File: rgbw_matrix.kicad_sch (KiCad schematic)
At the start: 34 parts, among them IC1 TLC59283DBQR, IC2 TLC59283DBQR, IC3 TLC59283DBQR, IC4 TLC59283DBQR, IC5 TLC59283DBQR, IC6 TLC59283DBQR

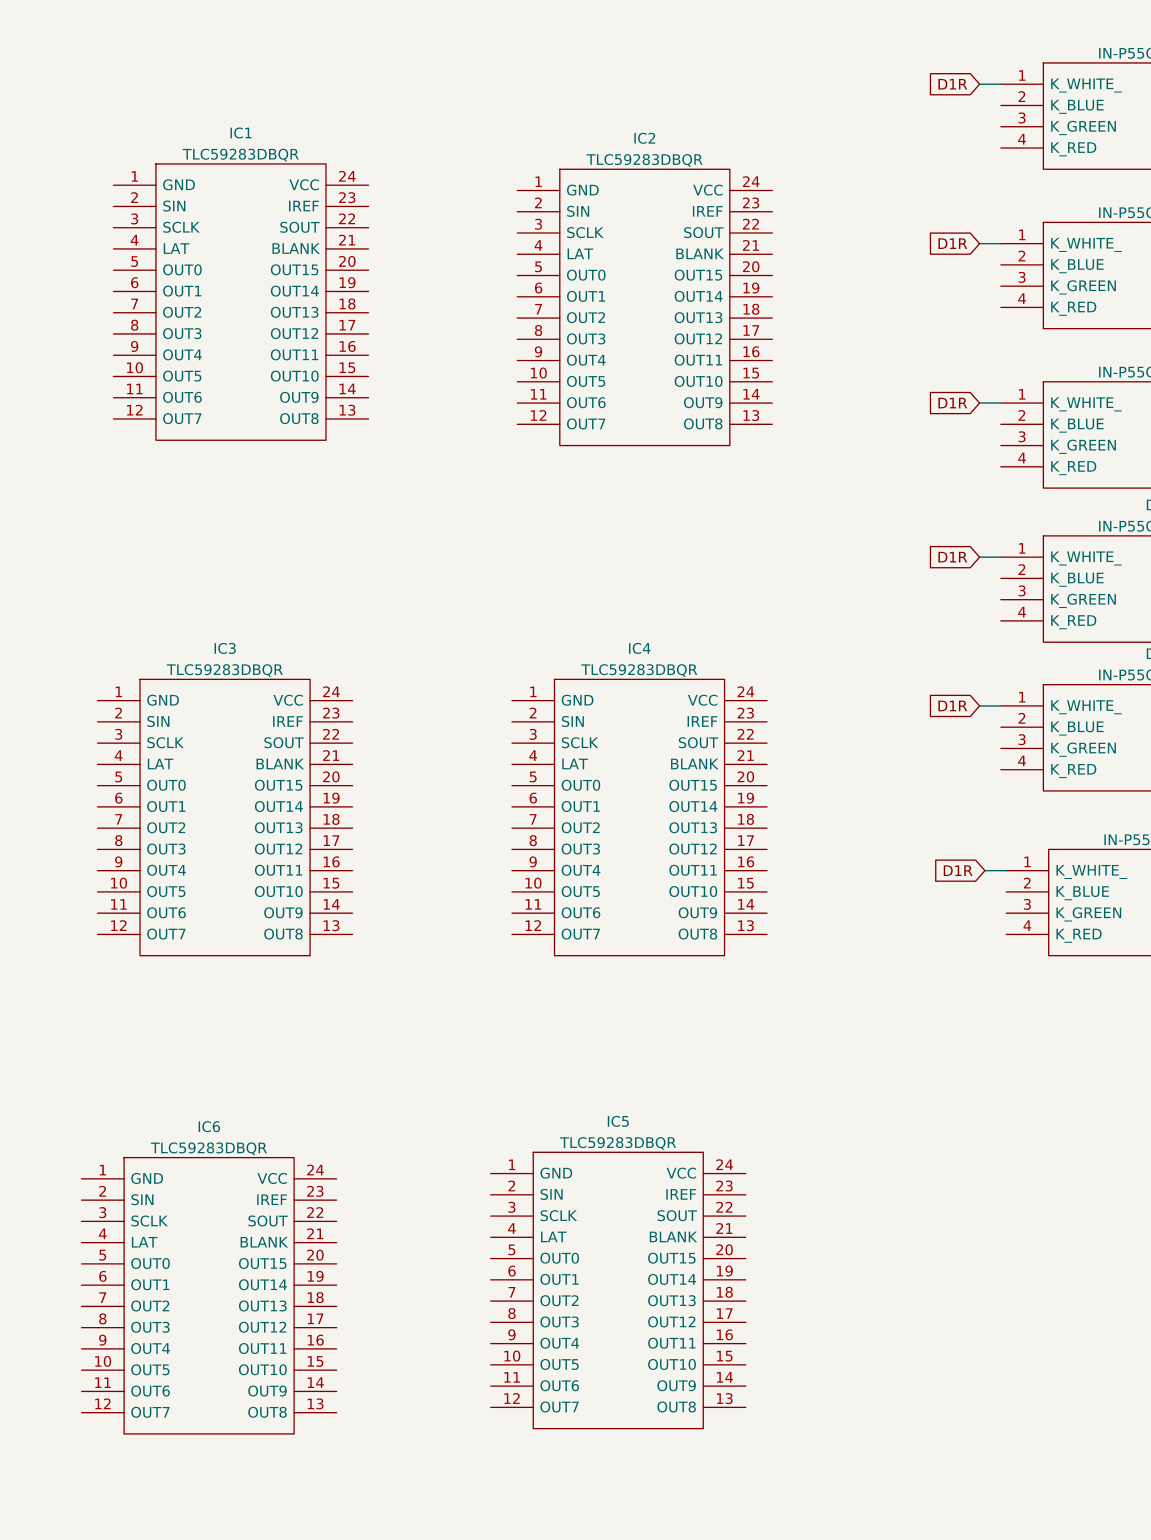
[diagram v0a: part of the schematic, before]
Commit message: Did a little more schematic routing
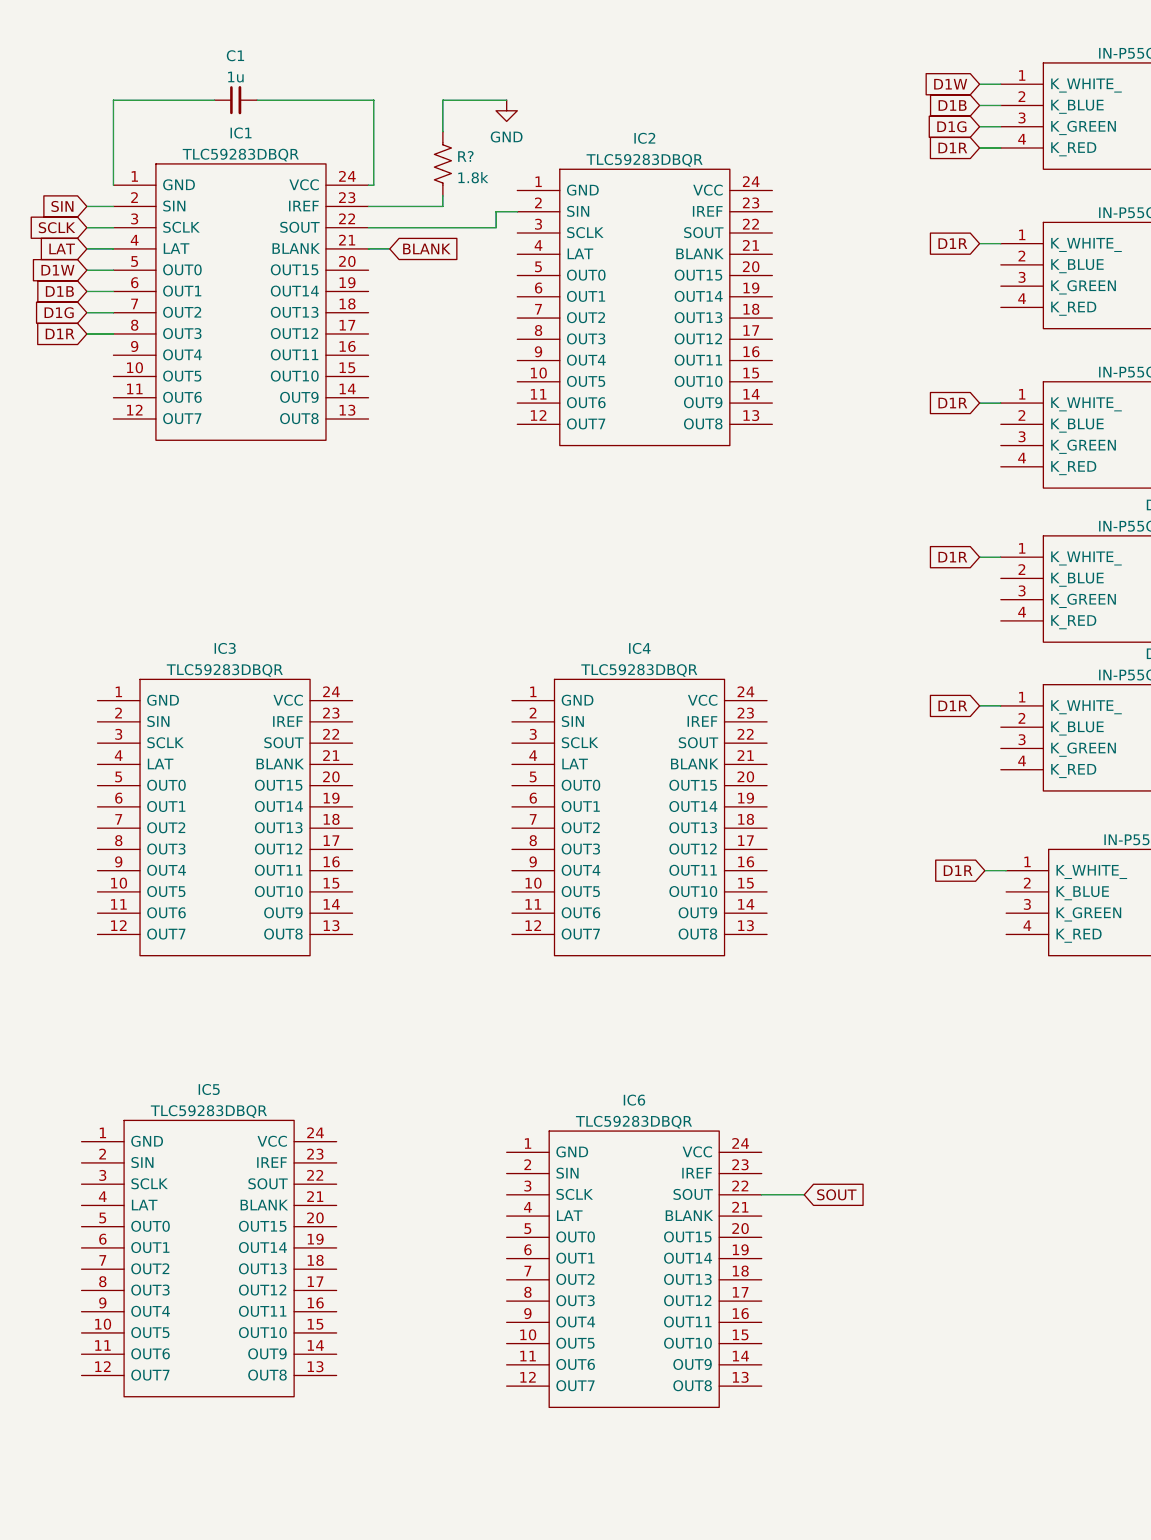
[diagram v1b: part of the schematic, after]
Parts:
- added C1: 1u, symbol Device:C_Small
- added R?: 1.8k, symbol Device:R_US
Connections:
- net D1R: now also D1.4 (K_RED), IC1.8 (OUT3); no longer D1.1 (K_WHITE_)
- net at IC2.2 (SIN): now also IC1.22 (SOUT)
- net at IC1.1 (GND): now also C1.1
- net SIN: now reaches IC1.2 (SIN)
- net BLANK: now reaches IC1.21 (BLANK)
- net at IC1.23 (IREF): now also R?.2
- net at IC1.24 (VCC): now also C1.2
- net SCLK: now reaches IC1.3 (SCLK)
- net LAT: now reaches IC1.4 (LAT)
- net D1W: now reaches IC1.5 (OUT0)
- net D1W: now also D1.1 (K_WHITE_)
- net D1B: now reaches IC1.6 (OUT1)
- net D1B: now also D1.2 (K_BLUE)
- net D1G: now reaches IC1.7 (OUT2)
- net D1G: now also D1.3 (K_GREEN)
- net SOUT: now reaches IC6.22 (SOUT)
- new net GND: R?.1
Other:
- moved on the sheet: IC5, IC6

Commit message: components connected v1
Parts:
- removed R?: 1.8k, symbol Device:R_US
- added C2, C3, C4, C5, C6: 1u, Capacitor_SMD:C_0201_0603Metric, symbol Device:C_Small
- added J1: Conn_01x07_Female, Connector_PinHeader_2.54mm:PinHeader_1x07_P2.54mm_Vertical, symbol Connector:Conn_01x07_Female
- added R1, R2, R3, R4, R5, R6: 1.8k, Resistor_SMD:R_0201_0603Metric, symbol Device:1.8k
- C1: footprint (none) -> Capacitor_SMD:C_0201_0603Metric
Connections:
- net BLANK: now also IC2.21 (BLANK), IC3.21 (BLANK), IC4.21 (BLANK), IC5.21 (BLANK), IC6.21 (BLANK), J1.2 (Pin_2)
- net D1R: no longer D10.1 (K_WHITE_), D11.1 (K_WHITE_), D12.1 (K_WHITE_), D13.1 (K_WHITE_), D14.1 (K_WHITE_), D15.1 (K_WHITE_), D16.1 (K_WHITE_), D17.1 (K_WHITE_), D18.1 (K_WHITE_), D19.1 (K_WHITE_), D2.1 (K_WHITE_), D20.1 (K_WHITE_), D21.1 (K_WHITE_), D22.1 (K_WHITE_), D23.1 (K_WHITE_), D24.1 (K_WHITE_), D3.1 (K_WHITE_), D4.1 (K_WHITE_), D5.1 (K_WHITE_), D6.1 (K_WHITE_), D7.1 (K_WHITE_), D8.1 (K_WHITE_), D9.1 (K_WHITE_)
- net GND: now also IC1.1 (GND), IC2.1 (GND), IC3.1 (GND), IC4.1 (GND), IC5.1 (GND), IC6.1 (GND), J1.7 (Pin_7), R1.1, R2.1, R3.1, R4.1, R5.1, R6.1
- net LAT: now also IC2.4 (LAT), IC3.4 (LAT), IC4.4 (LAT), IC5.4 (LAT), IC6.4 (LAT), J1.4 (Pin_4)
- net SCLK: now also IC2.3 (SCLK), IC3.3 (SCLK), IC4.3 (SCLK), IC5.3 (SCLK), IC6.3 (SCLK), J1.3 (Pin_3)
- net SIN: now also J1.5 (Pin_5)
- net SOUT: now also J1.6 (Pin_6)
- net VCC: now also C1.2, C2.2, C3.2, C4.2, C5.2, C6.2, J1.1 (Pin_1)
- net D21B: now reaches D21.2 (K_BLUE)
- net D21B: now also IC6.6 (OUT1)
- net D21G: now reaches D21.3 (K_GREEN)
- net D21G: now also IC6.7 (OUT2)
- net D21R: now reaches D21.4 (K_RED)
- net D21R: now also IC6.8 (OUT3)
- net D22B: now reaches D22.2 (K_BLUE)
- net D22B: now also IC6.10 (OUT5)
- net D22G: now reaches D22.3 (K_GREEN)
- net D22G: now also IC6.11 (OUT6)
- net D22R: now reaches D22.4 (K_RED)
- net D22R: now also IC6.12 (OUT7)
- net D11B: now reaches D11.2 (K_BLUE)
- net D11B: now also IC3.14 (OUT9)
- net D11G: now reaches D11.3 (K_GREEN)
- net D11G: now also IC3.15 (OUT10)
- net D11R: now reaches D11.4 (K_RED)
- net D11R: now also IC3.16 (OUT11)
- net D10B: now reaches IC3.10 (OUT5)
- net D10B: now also D10.2 (K_BLUE)
- net D10G: now reaches IC3.11 (OUT6)
- net D10G: now also D10.3 (K_GREEN)
- net D10R: now reaches IC3.12 (OUT7)
- net D10R: now also D10.4 (K_RED)
- net D11W: now reaches IC3.13 (OUT8)
- net D11W: now also D11.1 (K_WHITE_)
- net D12W: now reaches IC3.17 (OUT12)
- net D12W: now also D12.1 (K_WHITE_)
- net D12B: now reaches IC3.18 (OUT13)
- net D12B: now also D12.2 (K_BLUE)
- net D12G: now reaches IC3.19 (OUT14)
- net D12G: now also D12.3 (K_GREEN)
- net at IC3.2 (SIN): now also IC2.22 (SOUT)
- net D12R: now reaches IC3.20 (OUT15)
- net D12R: now also D12.4 (K_RED)
- net at IC3.22 (SOUT): now also IC4.2 (SIN)
- net at IC3.23 (IREF): now also R3.2
- net at IC3.24 (VCC): now also C3.1
- net D9W: now reaches IC3.5 (OUT0)
- net D9W: now also D9.1 (K_WHITE_)
- net D9B: now reaches IC3.6 (OUT1)
- net D9B: now also D9.2 (K_BLUE)
- net D9G: now reaches IC3.7 (OUT2)
- net D9G: now also D9.3 (K_GREEN)
- net D9R: now reaches IC3.8 (OUT3)
- net D9R: now also D9.4 (K_RED)
- net D10W: now reaches IC3.9 (OUT4)
- net D10W: now also D10.1 (K_WHITE_)
- net D3B: now reaches D3.2 (K_BLUE)
- net D3B: now also IC1.14 (OUT9)
- net D3G: now reaches D3.3 (K_GREEN)
- net D3G: now also IC1.15 (OUT10)
- net D3R: now reaches D3.4 (K_RED)
- net D3R: now also IC1.16 (OUT11)
- net D6B: now reaches IC2.10 (OUT5)
- net D6B: now also D6.2 (K_BLUE)
- net D6G: now reaches IC2.11 (OUT6)
- net D6G: now also D6.3 (K_GREEN)
- net D6R: now reaches IC2.12 (OUT7)
- net D6R: now also D6.4 (K_RED)
- net D7W: now reaches IC2.13 (OUT8)
- net D7W: now also D7.1 (K_WHITE_)
- net D7B: now reaches IC2.14 (OUT9)
- net D7B: now also D7.2 (K_BLUE)
- net D7G: now reaches IC2.15 (OUT10)
- net D7G: now also D7.3 (K_GREEN)
- net D7R: now reaches IC2.16 (OUT11)
- net D7R: now also D7.4 (K_RED)
- net D8W: now reaches IC2.17 (OUT12)
- net D8W: now also D8.1 (K_WHITE_)
- net D8B: now reaches IC2.18 (OUT13)
- net D8B: now also D8.2 (K_BLUE)
- net D8G: now reaches IC2.19 (OUT14)
- net D8G: now also D8.3 (K_GREEN)
- net D8R: now reaches IC2.20 (OUT15)
- net D8R: now also D8.4 (K_RED)
- net at IC2.23 (IREF): now also R2.2
- net at IC2.24 (VCC): now also C2.1
- net D5W: now reaches IC2.5 (OUT0)
- net D5W: now also D5.1 (K_WHITE_)
- net D5B: now reaches IC2.6 (OUT1)
- net D5B: now also D5.2 (K_BLUE)
- net D5G: now reaches IC2.7 (OUT2)
- net D5G: now also D5.3 (K_GREEN)
- net D5R: now reaches IC2.8 (OUT3)
- net D5R: now also D5.4 (K_RED)
- net D6W: now reaches IC2.9 (OUT4)
- net D6W: now also D6.1 (K_WHITE_)
- net D16B: now reaches D16.2 (K_BLUE)
- net D16B: now also IC4.18 (OUT13)
- net D16G: now reaches D16.3 (K_GREEN)
- net D16G: now also IC4.19 (OUT14)
- net D16R: now reaches D16.4 (K_RED)
- net D16R: now also IC4.20 (OUT15)
- net D19B: now reaches D19.2 (K_BLUE)
- net D19B: now also IC5.14 (OUT9)
- net D19G: now reaches D19.3 (K_GREEN)
- net D19G: now also IC5.15 (OUT10)
- net D19R: now reaches D19.4 (K_RED)
- net D19R: now also IC5.16 (OUT11)
- net at C1.1: now also IC1.24 (VCC); no longer IC1.1 (GND)
- net D2B: now reaches IC1.10 (OUT5)
- net D2B: now also D2.2 (K_BLUE)
- net D2G: now reaches IC1.11 (OUT6)
- net D2G: now also D2.3 (K_GREEN)
- net D2R: now reaches IC1.12 (OUT7)
- net D2R: now also D2.4 (K_RED)
- net D3W: now reaches IC1.13 (OUT8)
- net D3W: now also D3.1 (K_WHITE_)
- net D4W: now reaches IC1.17 (OUT12)
- net D4W: now also D4.1 (K_WHITE_)
- net D4B: now reaches IC1.18 (OUT13)
- net D4B: now also D4.2 (K_BLUE)
- net D4G: now reaches IC1.19 (OUT14)
- net D4G: now also D4.3 (K_GREEN)
- net D4R: now reaches IC1.20 (OUT15)
- net D4R: now also D4.4 (K_RED)
- net at IC1.23 (IREF): now also R1.2
- net D2W: now reaches IC1.9 (OUT4)
- net D2W: now also D2.1 (K_WHITE_)
- net D14B: now reaches D14.2 (K_BLUE)
- net D14B: now also IC4.10 (OUT5)
- net D14G: now reaches D14.3 (K_GREEN)
- net D14G: now also IC4.11 (OUT6)
- net D14R: now reaches D14.4 (K_RED)
- net D14R: now also IC4.12 (OUT7)
- net D18B: now reaches IC5.10 (OUT5)
- net D18B: now also D18.2 (K_BLUE)
- net D18G: now reaches IC5.11 (OUT6)
- net D18G: now also D18.3 (K_GREEN)
- net D18R: now reaches IC5.12 (OUT7)
- net D18R: now also D18.4 (K_RED)
- net D19W: now reaches IC5.13 (OUT8)
- net D19W: now also D19.1 (K_WHITE_)
- net D20W: now reaches IC5.17 (OUT12)
- net D20W: now also D20.1 (K_WHITE_)
- net D20B: now reaches IC5.18 (OUT13)
- net D20B: now also D20.2 (K_BLUE)
- net D20G: now reaches IC5.19 (OUT14)
- net D20G: now also D20.3 (K_GREEN)
- net at IC5.2 (SIN): now also IC4.22 (SOUT)
- net D20R: now reaches IC5.20 (OUT15)
- net D20R: now also D20.4 (K_RED)
- net at IC5.22 (SOUT): now also IC6.2 (SIN)
- net at IC5.23 (IREF): now also R5.2
- net at IC5.24 (VCC): now also C5.1
- net D17W: now reaches IC5.5 (OUT0)
- net D17W: now also D17.1 (K_WHITE_)
- net D17B: now reaches IC5.6 (OUT1)
- net D17B: now also D17.2 (K_BLUE)
- net D17G: now reaches IC5.7 (OUT2)
- net D17G: now also D17.3 (K_GREEN)
- net D17R: now reaches IC5.8 (OUT3)
- net D17R: now also D17.4 (K_RED)
- net D18W: now reaches IC5.9 (OUT4)
- net D18W: now also D18.1 (K_WHITE_)
- net D15W: now reaches IC4.13 (OUT8)
- net D15W: now also D15.1 (K_WHITE_)
- net D15B: now reaches IC4.14 (OUT9)
- net D15B: now also D15.2 (K_BLUE)
- net D15G: now reaches IC4.15 (OUT10)
- net D15G: now also D15.3 (K_GREEN)
- net D15R: now reaches IC4.16 (OUT11)
- net D15R: now also D15.4 (K_RED)
- net D16W: now reaches IC4.17 (OUT12)
- net D16W: now also D16.1 (K_WHITE_)
- net at IC4.23 (IREF): now also R4.2
- net at IC4.24 (VCC): now also C4.1
- net D13W: now reaches IC4.5 (OUT0)
- net D13W: now also D13.1 (K_WHITE_)
- net D13B: now reaches IC4.6 (OUT1)
- net D13B: now also D13.2 (K_BLUE)
- net D13G: now reaches IC4.7 (OUT2)
- net D13G: now also D13.3 (K_GREEN)
- net D13R: now reaches IC4.8 (OUT3)
- net D13R: now also D13.4 (K_RED)
- net D14W: now reaches IC4.9 (OUT4)
- net D14W: now also D14.1 (K_WHITE_)
- net D23W: now reaches IC6.13 (OUT8)
- net D23W: now also D23.1 (K_WHITE_)
- net D23B: now reaches IC6.14 (OUT9)
- net D23B: now also D23.2 (K_BLUE)
- net D23G: now reaches IC6.15 (OUT10)
- net D23G: now also D23.3 (K_GREEN)
- net D23R: now reaches IC6.16 (OUT11)
- net D23R: now also D23.4 (K_RED)
- net D24W: now reaches IC6.17 (OUT12)
- net D24W: now also D24.1 (K_WHITE_)
- net D24B: now reaches IC6.18 (OUT13)
- net D24B: now also D24.2 (K_BLUE)
- net D24G: now reaches IC6.19 (OUT14)
- net D24G: now also D24.3 (K_GREEN)
- net D24R: now reaches IC6.20 (OUT15)
- net D24R: now also D24.4 (K_RED)
- net at IC6.23 (IREF): now also R6.2
- net at IC6.24 (VCC): now also C6.1
- net D21W: now reaches IC6.5 (OUT0)
- net D21W: now also D21.1 (K_WHITE_)
- net D22W: now reaches IC6.9 (OUT4)
- net D22W: now also D22.1 (K_WHITE_)
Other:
- moved on the sheet: C1, D1, D10, D11, D12, D13, D14, D15, D16, D17, D18, D19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

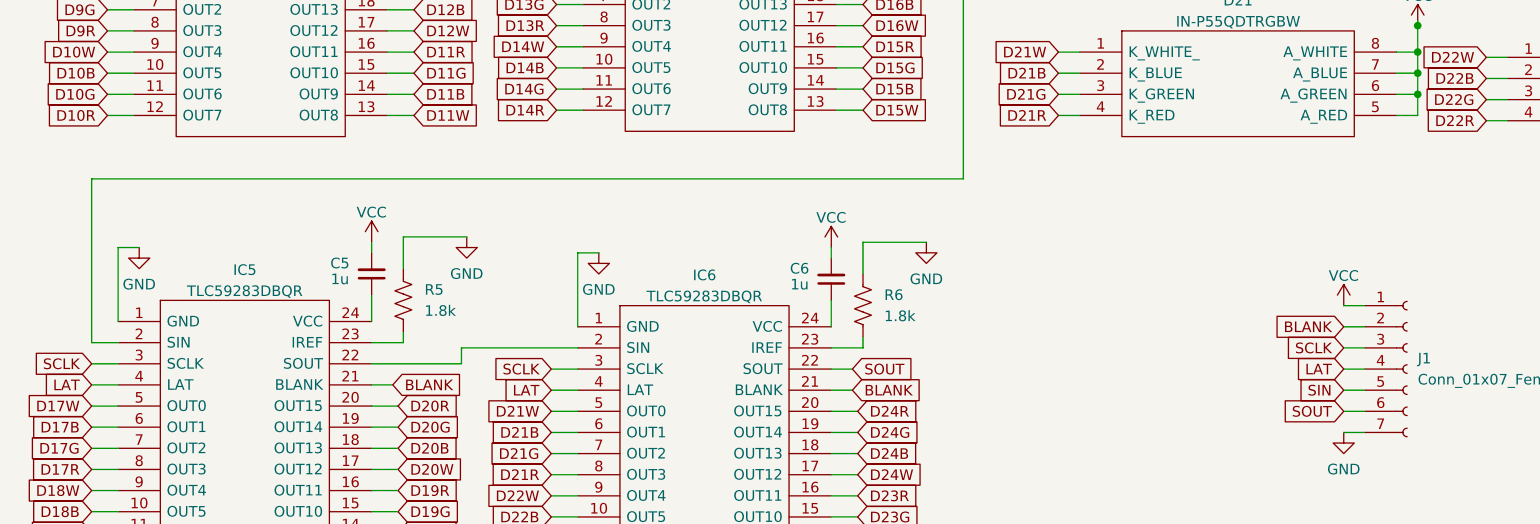
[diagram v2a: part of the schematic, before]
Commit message: Added power flag, corrected capacitor on one chip need to do the others
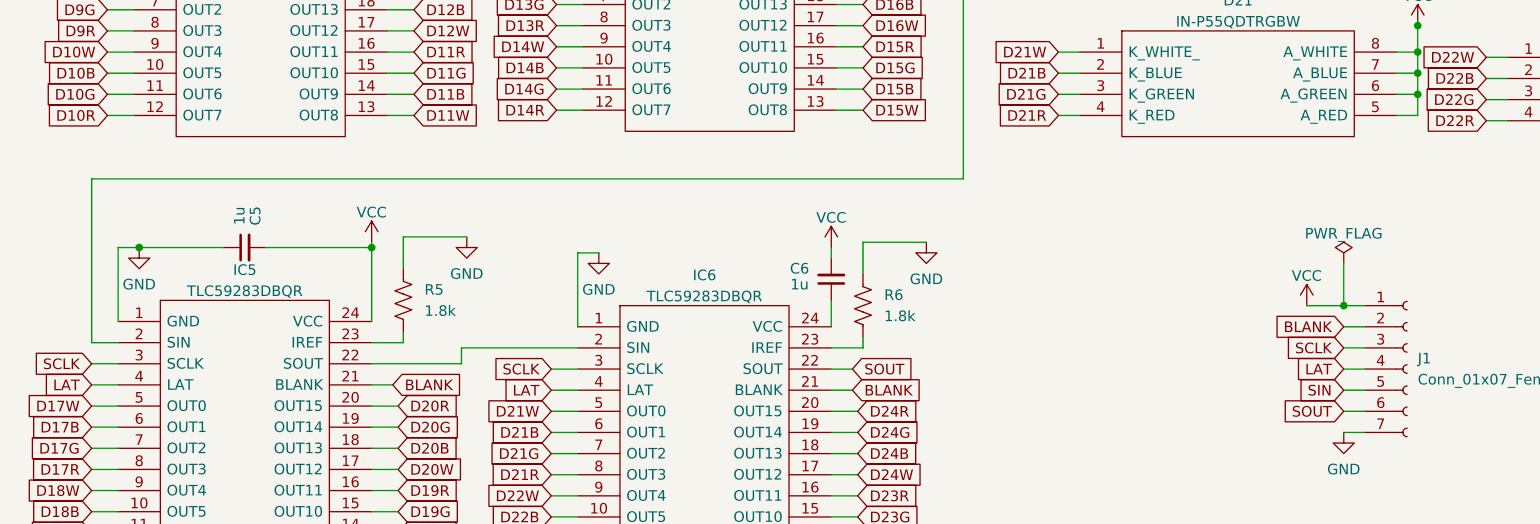
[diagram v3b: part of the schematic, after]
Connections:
- net GND: now also C5.1
- net VCC: now also IC5.24 (VCC)
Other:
- moved on the sheet: C5
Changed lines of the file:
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@@
   (junction (at 180.975 62.23) (diameter 0) (color 0 0 0 0)
   )
+  (junction (at 55.88 141.605) (diameter 0) (color 0 0 0 0)
+  )
+  (junction (at 27.94 141.605) (diameter 0) (color 0 0 0 0)
+  )
   (junction (at 233.045 123.825) (diameter 0) (color 0 0 0 0)
   )
@@
   (junction (at 335.28 40.64) (diameter 0) (color 0 0 0 0)
   )
+  (junction (at 172.72 148.59) (diameter 0) (color 0 0 0 0)
+  )
   (junction (at 335.28 65.405) (diameter 0) (color 0 0 0 0)
   )
@@
     (stroke (width 0) (type default) (color 0 0 0 0))
   )
-  (wire (pts (xy 172.72 148.59) (xy 175.26 148.59))
+  (wire (pts (xy 168.275 148.59) (xy 172.72 148.59))
     (stroke (width 0) (type default) (color 0 0 0 0))
   )
@@
     (stroke (width 0) (type default) (color 0 0 0 0))
   )
+  (wire (pts (xy 172.72 148.59) (xy 175.26 148.59))
+    (stroke (width 0) (type default) (color 0 0 0 0))
+  )
   (wire (pts (xy 232.41 86.36) (xy 229.87 86.36))
     (stroke (width 0) (type default) (color 0 0 0 0))
@@
     (stroke (width 0) (type default) (color 0 0 0 0))
   )
+  (wire (pts (xy 43.18 141.605) (xy 55.88 141.605))
+    (stroke (width 0) (type default) (color 0 0 0 0))
+  )
   (wire (pts (xy 69.85 38.735) (xy 81.28 38.735))
     (stroke (width 0) (type default) (color 0 0 0 0))
@@
     (stroke (width 0) (type default) (color 0 0 0 0))
   )
-  (wire (pts (xy 55.88 140.97) (xy 55.88 142.24))
+  (wire (pts (xy 55.88 140.97) (xy 55.88 141.605))
     (stroke (width 0) (type default) (color 0 0 0 0))
   )
@@
     (stroke (width 0) (type default) (color 0 0 0 0))
   )
+  (wire (pts (xy 172.72 143.51) (xy 172.72 148.59))
+    (stroke (width 0) (type default) (color 0 0 0 0))
+  )
   (wire (pts (xy 335.28 27.305) (xy 335.28 29.845))
     (stroke (width 0) (type default) (color 0 0 0 0))
@@
     (stroke (width 0) (type default) (color 0 0 0 0))
   )
-  (wire (pts (xy 55.88 147.32) (xy 55.88 150.495))
+  (wire (pts (xy 55.88 141.605) (xy 55.88 150.495))
     (stroke (width 0) (type default) (color 0 0 0 0))
   )
@@
     (stroke (width 0) (type default) (color 0 0 0 0))
   )
+  (wire (pts (xy 27.94 141.605) (xy 38.1 141.605))
+    (stroke (width 0) (type default) (color 0 0 0 0))
+  )
   (wire (pts (xy 137.795 45.72) (xy 140.335 45.72))
     (stroke (width 0) (type default) (color 0 0 0 0))
@@
     (pin "1")
   )
-  (symbol (lib_id "power:VCC") (at 172.72 148.59 0) (unit 1)
+  (symbol (lib_id "power:VCC") (at 168.275 148.59 0) (unit 1)
     (in_bom yes) (on_board yes) (fields_autoplaced)
-    (property "Reference" "#PWR0108" (id 0) (at 172.72 152.4 0)
+    (property "Reference" "#PWR0108" (id 0) (at 168.275 152.4 0)
       (effects (font (size 1.27 1.27)) hide)
     )
-    (property "Value" "VCC" (id 1) (at 172.72 145.0142 0))
-    (property "Footprint" "" (id 2) (at 172.72 148.59 0)
+    (property "Value" "VCC" (id 1) (at 168.275 145.0142 0))
+    (property "Footprint" "" (id 2) (at 168.275 148.59 0)
       (effects (font (size 1.27 1.27)) hide)
     )
-    (property "Datasheet" "" (id 3) (at 172.72 148.59 0)
+    (property "Datasheet" "" (id 3) (at 168.275 148.59 0)
       (effects (font (size 1.27 1.27)) hide)
     )
@@
     (pin "9")
   )
-  (symbol (lib_name "C_Small_1") (lib_id "Device:C_Small") (at 55.88 144.78 180) (unit 1)
+  (symbol (lib_name "C_Small_1") (lib_id "Device:C_Small") (at 40.64 141.605 90) (unit 1)
     (in_bom yes) (on_board yes)
-    (property "Reference" "C5" (id 0) (at 52.07 143.51 0))
-    (property "Value" "1u" (id 1) (at 52.07 145.415 0))
-    (property "Footprint" "Capacitor_SMD:C_0201_0603Metric" (id 2) (at 55.88 144.78 90)
+    (property "Reference" "C5" (id 0) (at 41.91 137.795 0))
+    (property "Value" "1u" (id 1) (at 40.005 137.795 0))
+    (property "Footprint" "Capacitor_SMD:C_0201_0603Metric" (id 2) (at 40.64 141.605 90)
       (effects (font (size 1.27 1.27)) hide)
     )
-    (property "Datasheet" "~" (id 3) (at 55.88 144.78 0)
+    (property "Datasheet" "~" (id 3) (at 40.64 141.605 0)
       (effects (font (size 1.27 1.27)) hide)
     )
@@
     (pin "8")
   )
+  (symbol (lib_id "power:PWR_FLAG") (at 172.72 143.51 0) (unit 1)
+    (in_bom yes) (on_board yes) (fields_autoplaced)
+    (property "Reference" "#FLG0101" (id 0) (at 172.72 141.605 0)
+      (effects (font (size 1.27 1.27)) hide)
+    )
+    (property "Value" "PWR_FLAG" (id 1) (at 172.72 139.9342 0))
+    (property "Footprint" "" (id 2) (at 172.72 143.51 0)
+      (effects (font (size 1.27 1.27)) hide)
+    )
+    (property "Datasheet" "~" (id 3) (at 172.72 143.51 0)
+      (effects (font (size 1.27 1.27)) hide)
+    )
+    (pin "1")
+  )
   (symbol (lib_id "power:VCC") (at 283.845 59.69 0) (unit 1)
     (in_bom yes) (on_board yes) (fields_autoplaced)
@@
   )
   (symbol_instances
+    (path "/cce835e8-6027-45eb-8d04-ebc4fcb4349e"
+      (reference "#FLG0101") (unit 1) (value "PWR_FLAG") (footprint "")
+    )
     (path "/c1065384-b958-4aee-9c33-6ee90905debb"
       (reference "#PWR01") (unit 1) (value "VCC") (footprint "")
